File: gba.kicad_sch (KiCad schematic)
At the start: 1 part

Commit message: Modified STM32 Symbol: - moved supply in seperate unit
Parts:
- removed IC?: STM32MP151AAC3, STM32MP151AAC3, symbol SamacSys_Parts:STM32MP151AAC3
- added IC1: STM32MP157AAB3, ARMband:BGA354C80P19X19_1600X1600X129, symbol ARMband:STM32MP157AAB3_(modified)
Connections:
- new net: IC1., IC1.T16 (PA10)

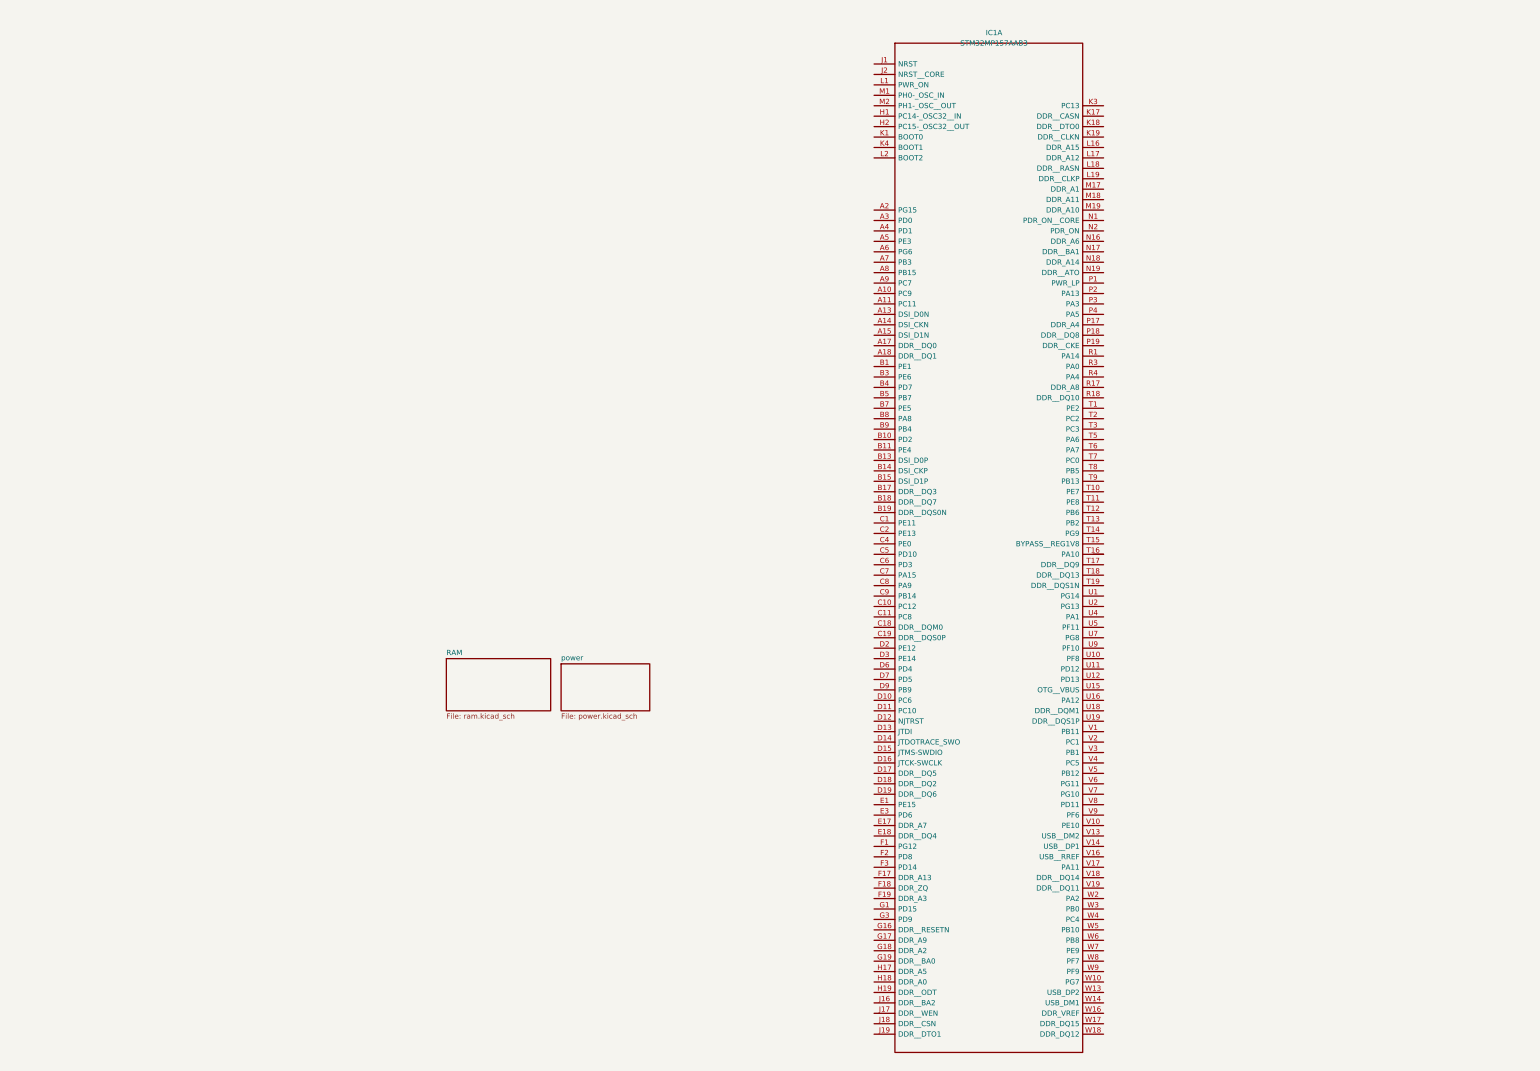
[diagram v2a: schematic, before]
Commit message: Connected power rails to mp1
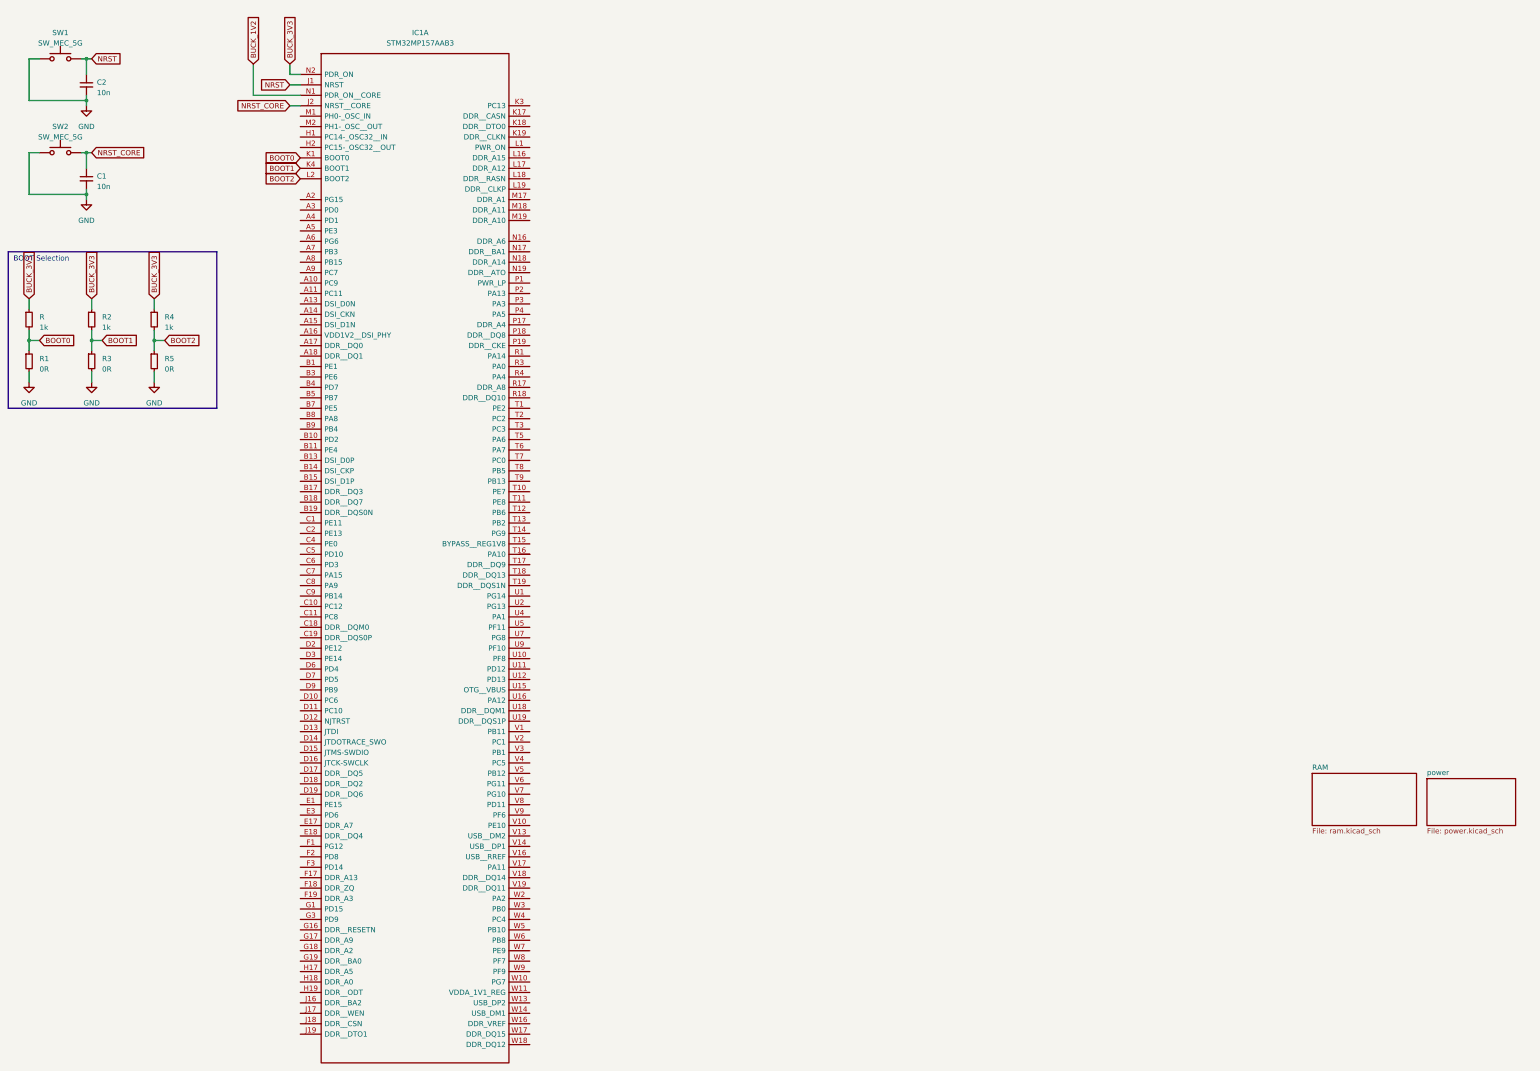
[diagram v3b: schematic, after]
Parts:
- added C1, C2: 10n, symbol Device:C_Small
- added R, R2, R4: 1k, symbol Device:R_Small
- added R1, R3, R5: 0R, symbol Device:R_Small
- added SW1, SW2: SW_MEC_5G, symbol Switch:SW_MEC_5G
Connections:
- net NRST: now reaches IC1.J1 (NRST)
- net NRST: now also C2.1, SW1.3 (B), SW1.4 (B)
- net NRST_CORE: now reaches IC1.J2 (NRST__CORE)
- net NRST_CORE: now also C1.1, SW2.3 (B), SW2.4 (B)
- net BOOT0: now reaches IC1.K1 (BOOT0)
- net BOOT0: now also R.2, R1.1
- net BOOT1: now reaches IC1.K4 (BOOT1)
- net BOOT1: now also R2.2, R3.1
- net BOOT2: now reaches IC1.L2 (BOOT2)
- net BOOT2: now also R4.2, R5.1
- net BUCK_1V2: now reaches IC1.N1 (PDR_ON__CORE)
- net BUCK_3V3: now reaches IC1.N2 (PDR_ON)
- net BUCK_3V3: now also R.1, R2.1, R4.1
- new net GND: C1.2, C2.2, R1.2, R3.2, R5.2, SW1.1 (A), SW1.2 (A), SW2.1 (A), SW2.2 (A)
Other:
- note added: "BOOT Selection"

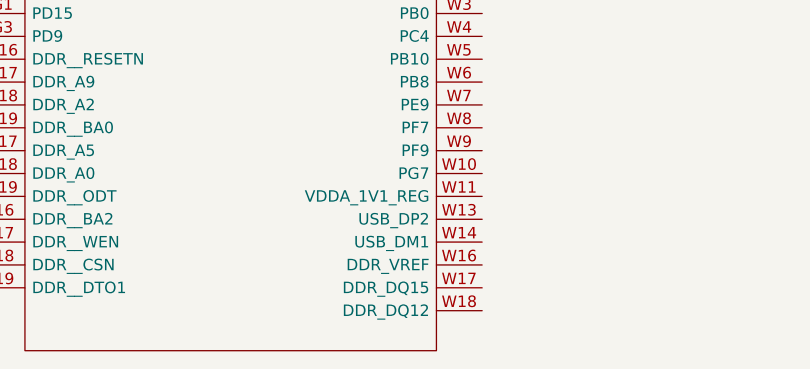
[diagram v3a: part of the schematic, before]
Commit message: added VREV_DDR
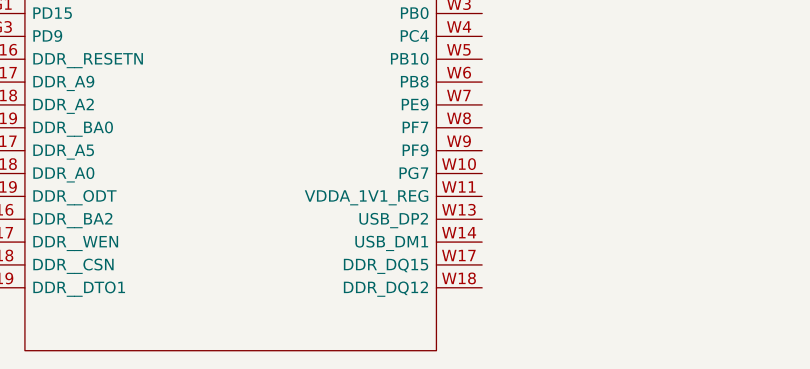
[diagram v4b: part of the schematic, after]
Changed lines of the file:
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@@
     (pin "W13")
     (pin "W14")
-    (pin "W16")
     (pin "W17")
     (pin "W18")
@@
     (pin "W12")
     (pin "W15")
+    (pin "W16")
     (pin "W19")
     (instances

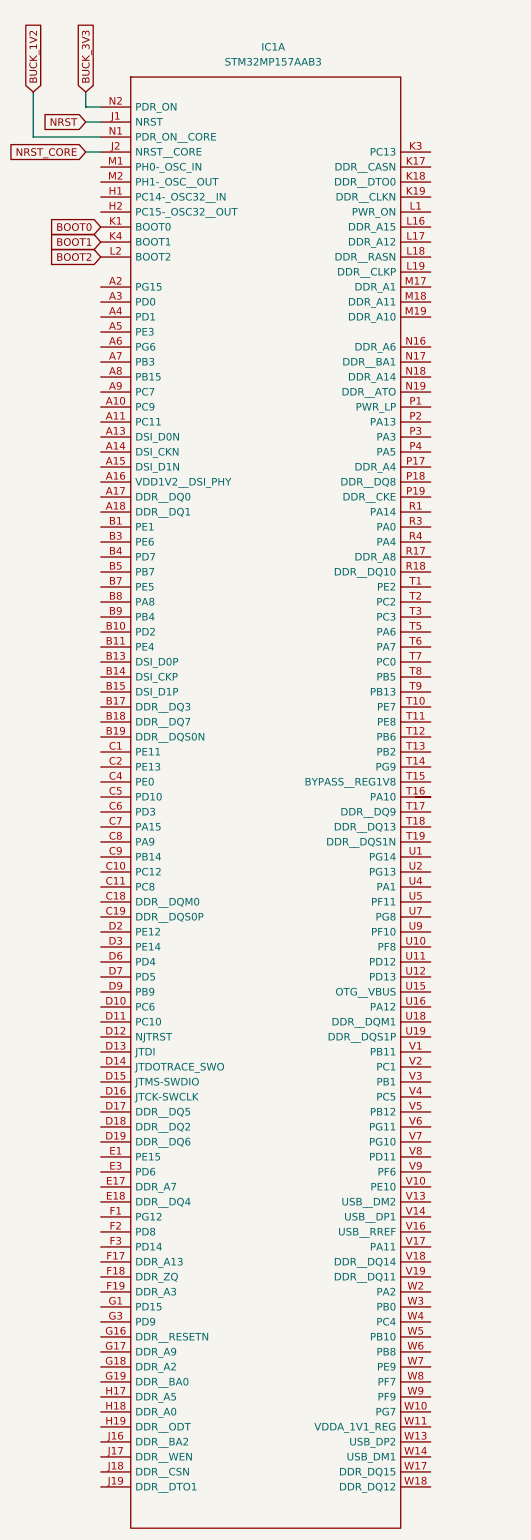
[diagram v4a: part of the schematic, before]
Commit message: Updated Symbols + Added Supply connections
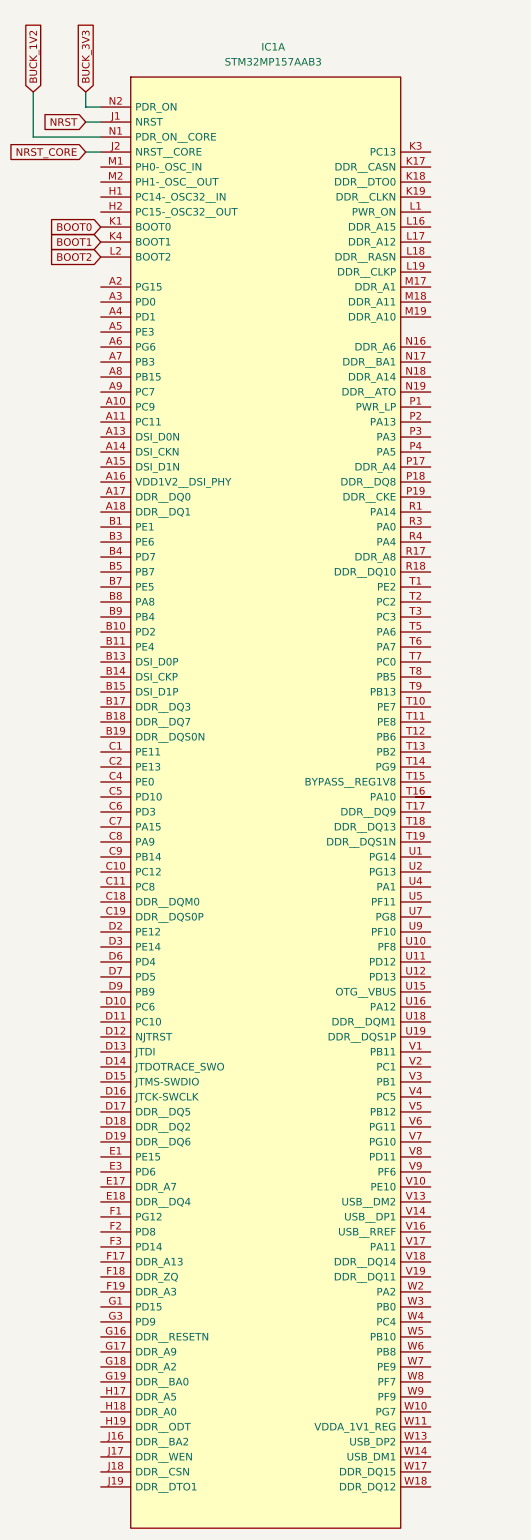
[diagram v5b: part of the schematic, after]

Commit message: Added eMMC (S40FC004C1B2C00000)
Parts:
- added IC7: S40FC004C1B2C00000, BGA153C50P14X14_900X750X80, symbol ARMband:S40FC004C1B2C00000
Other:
- note added: "TODO: Split power"
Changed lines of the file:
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@@
     (stroke (width 0) (type default))
   )
-  (polyline (pts (xy 63.5 114.3) (xy 63.5 76.2))
+  (polyline (pts (xy 66.04 114.3) (xy 66.04 73.66))
     (stroke (width 0) (type default))
   )
@@
     (stroke (width 0) (type default))
   )
-  (polyline (pts (xy 12.7 76.2) (xy 12.7 114.3))
+  (polyline (pts (xy 12.7 73.66) (xy 12.7 114.3))
     (stroke (width 0) (type default))
   )
@@
     (stroke (width 0) (type default))
   )
-  (polyline (pts (xy 12.7 114.3) (xy 63.5 114.3))
+  (polyline (pts (xy 12.7 114.3) (xy 66.04 114.3))
     (stroke (width 0) (type default))
   )
@@
     (stroke (width 0) (type default))
   )
-  (polyline (pts (xy 12.7 76.2) (xy 63.5 76.2))
+  (polyline (pts (xy 12.7 73.66) (xy 66.04 73.66))
     (stroke (width 0) (type default))
   )
@@
     (stroke (width 0) (type default))
   )
-  (text "BOOT Selection" (at 13.97 78.74 0)
+  (text "BOOT Selection" (at 50.8 76.2 0)
+    (effects (font (size 1.27 1.27)) (justify left bottom))
+  )
+  (text "TODO: Split power" (at 264.16 38.1 0)
     (effects (font (size 1.27 1.27)) (justify left bottom))
   )
@@
         )
       )
+    )
+  )
+  (symbol (lib_id "ARMband:S40FC004C1B2C00000") (at 266.7 43.18 0) (unit 1)
+    (in_bom yes) (on_board yes) (dnp no) (fields_autoplaced)
+    (property "Reference" "IC7" (at 246.38 36.4109 0)
+      (effects (font (size 1.27 1.27)))
+    )
+    (property "Value" "S40FC004C1B2C00000" (at 246.38 38.3319 0)
+      (effects (font (size 1.27 1.27)))
+    )
+    (property "Footprint" "BGA153C50P14X14_900X750X80" (at 295.91 40.64 0)
+      (effects (font (size 1.27 1.27)) (justify left) hide)
+    )
+    (property "Datasheet" "http://www.skyhighmemory.com/download/dataSheet/002-01112.pdf" (at 295.91 43.18 0)
+      (effects (font (size 1.27 1.27)) (justify left) hide)
+    )
+    (property "Description" "eMMC 4GB, 3.3 V, e.MMC Flash" (at 295.91 45.72 0)
+      (effects (font (size 1.27 1.27)) (justify left) hide)
+    )
+    (property "Height" "0.8" (at 332.74 63.5 0)
+      (effects (font (size 1.27 1.27)) (justify left) hide)
+    )
+    (property "Mouser Part Number" "727-S40FC004C1B2C000" (at 332.74 66.04 0)
+      (effects (font (size 1.27 1.27)) (justify left) hide)
+    )
+    (property "Mouser Price/Stock" "https://www.mouser.co.uk/ProductDetail/SkyHigh-Memory/S40FC004C1B2C00000?qs=OlC7AqGiEDnnqQ4BF5kidg%3D%3D" (at 295.91 53.34 0)
+      (effects (font (size 1.27 1.27)) (justify left) hide)
+    )
+    (property "Manufacturer_Name" "SkyHigh Memory" (at 332.74 71.12 0)
+      (effects (font (size 1.27 1.27)) (justify left) hide)
+    )
+    (property "Manufacturer_Part_Number" "S40FC004C1B2C00000" (at 332.74 73.66 0)
+      (effects (font (size 1.27 1.27)) (justify left) hide)
+    )
+    (pin "A1")
+    (pin "A10")
+    (pin "A11")
+    (pin "A12")
+    (pin "A13")
+    (pin "A14")
+    (pin "A2")
+    (pin "A3")
+    (pin "A4")
+    (pin "A5")
+    (pin "A6")
+    (pin "A7")
+    (pin "A8")
+    (pin "A9")
+    (pin "B1")
+    (pin "B10")
+    (pin "B11")
+    (pin "B12")
+    (pin "B13")
+    (pin "B14")
+    (pin "B2")
+    (pin "B3")
+    (pin "B4")
+    (pin "B5")
+    (pin "B6")
+    (pin "B7")
+    (pin "B8")
+    (pin "B9")
+    (pin "C1")
+    (pin "C10")
+    (pin "C11")
+    (pin "C12")
+    (pin "C13")
+    (pin "C14")
+    (pin "C2")
+    (pin "C3")
+    (pin "C4")
+    (pin "C5")
+    (pin "C6")
+    (pin "C7")
+    (pin "C8")
+    (pin "C9")
+    (pin "D1")
+    (pin "D12")
+    (pin "D13")
+    (pin "D14")
+    (pin "D2")
+    (pin "D3")
+    (pin "D4")
+    (pin "E1")
+    (pin "E10")
+    (pin "E12")
+    (pin "E13")
+    (pin "E14")
+    (pin "E2")
+    (pin "E3")
+    (pin "E5")
+    (pin "E6")
+    (pin "E7")
+    (pin "E8")
+    (pin "E9")
+    (pin "F1")
+    (pin "F10")
+    (pin "F12")
+    (pin "F13")
+    (pin "F14")
+    (pin "F2")
+    (pin "F3")
+    (pin "F5")
+    (pin "G1")
+    (pin "G10")
+    (pin "G12")
+    (pin "G13")
+    (pin "G14")
+    (pin "G2")
+    (pin "G3")
+    (pin "G5")
+    (pin "H1")
+    (pin "H10")
+    (pin "H12")
+    (pin "H13")
+    (pin "H14")
+    (pin "H2")
+    (pin "H3")
+    (pin "H5")
+    (pin "J1")
+    (pin "J10")
+    (pin "J12")
+    (pin "J13")
+    (pin "J14")
+    (pin "J2")
+    (pin "J3")
+    (pin "J5")
+    (pin "K1")
+    (pin "K10")
+    (pin "K12")
+    (pin "K13")
+    (pin "K14")
+    (pin "K2")
+    (pin "K3")
+    (pin "K5")
+    (pin "K6")
+    (pin "K7")
+    (pin "K8")
+    (pin "K9")
+    (pin "L1")
+    (pin "L12")
+    (pin "L13")
+    (pin "L14")
+    (pin "L2")
+    (pin "L3")
+    (pin "M1")
+    (pin "M10")
+    (pin "M11")
+    (pin "M12")
+    (pin "M13")
+    (pin "M14")
+    (pin "M2")
+    (pin "M3")
+    (pin "M4")
+    (pin "M5")
+    (pin "M6")
+    (pin "M7")
+    (pin "M8")
+    (pin "M9")
+    (pin "N1")
+    (pin "N10")
+    (pin "N11")
+    (pin "N12")
+    (pin "N13")
+    (pin "N14")
+    (pin "N2")
+    (pin "N3")
+    (pin "N4")
+    (pin "N5")
+    (pin "N6")
+    (pin "N7")
+    (pin "N8")
+    (pin "N9")
+    (pin "P1")
+    (pin "P10")
+    (pin "P11")
+    (pin "P12")
+    (pin "P13")
+    (pin "P14")
+    (pin "P2")
+    (pin "P3")
+    (pin "P4")
+    (pin "P5")
+    (pin "P6")
+    (pin "P7")
+    (pin "P8")
+    (pin "P9")
+    (instances
+      (project "gba"
+        (path "/017c50c6-333c-4d31-ad5a-278994a09b14"
+          (reference "IC7") (unit 1)
+        )
+      )
